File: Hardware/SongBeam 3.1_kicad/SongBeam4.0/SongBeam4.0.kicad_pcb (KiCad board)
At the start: 2 copper layers, 130 parts, among them J1 Conn_01x02, J10 732511150, J11 USB_B_Micro, J12 Conn_01x02, J13 Conn_01x02, J2 RJ45, J3 RJ45, J4 Conn_01x07, J5 Conn_01x04, J6 Conn_01x07, J7 Conn_01x09, J8 Conn_01x04, J9 Conn_01x08, SW2 PTS815 SJM 250 SMTR LFS, SW3 PTS815 SJM 250 SMTR LFS, U1 IM66D132H, U10 Teensy4.1, U11 BQ25185, U12 AO6604, U13 TPS62842DGRR, U14 TPL5111DDCR, U15 AO6604, U16 TXS0108EPW, U17 LP5907MFX-1.8/NOPB, U18 AO3407A, U19 MAX-M10M-00B, U2 IM66D132H, U3 IM66D132H, U4 IM66D132H, U5 IM66D132H, U6 IM66D132H, U7 IM66D132H, U8 IM66D132H, U9 PCMD3180IRTWR

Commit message: pcb savepoint
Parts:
- removed J13: Conn_01x02, Connector_PinHeader_1.00mm:PinHeader_1x02_P1.00mm_Horizontal
- added REF3: MountingHole_3.2mm_M3, MountingHole:MountingHole_3.2mm_M3, F.Cu at (193.5, 31.0)
- added REF3: MountingHole_3.2mm_M3, MountingHole:MountingHole_3.2mm_M3, F.Cu at (26.6, 30.9)
- added REF3: MountingHole_3.2mm_M3, MountingHole:MountingHole_3.2mm_M3, F.Cu at (26.7, 127.0)
- added REF3: MountingHole_3.2mm_M3, MountingHole:MountingHole_3.2mm_M3, F.Cu at (193.6, 127.0)
- CHG1: value ORANGE -> SFH2701; footprint LED_SMD:LED_0201_0603Metric -> LED_SMD:LED-APA102-2020
- D4, D5, D6: value MBRX120 -> MBRX120LF-TP
- Fault1: renamed from FAULT1; value RED -> SFH2701; footprint LED_SMD:LED_0201_0603Metric -> LED_SMD:LED-APA102-2020
- J10: footprint DFE201612E:1286ASH1R0MP2 -> 73251:CONN_73251-1150_MOL
- J11: value USB_B_Micro -> Conn_01x02; footprint 10118192:101181920002LF -> Connector_PinHeader_1.00mm:PinHeader_1x02_P1.00mm_Horizontal
- J7: value Conn_01x09 -> Conn_01x04; footprint Connector_PinHeader_1.00mm:PinHeader_1x09_P1.00mm_Horizontal -> Connector_PinHeader_1.00mm:PinHeader_1x04_P1.00mm_Horizontal
- J8: value Conn_01x04 -> Conn_01x08; footprint Connector_PinHeader_1.00mm:PinHeader_1x04_P1.00mm_Horizontal -> Connector_PinHeader_1.00mm:PinHeader_1x08_P1.00mm_Horizontal
- J9: value Conn_01x08 -> USB_B_Micro; footprint Connector_PinHeader_1.00mm:PinHeader_1x08_P1.00mm_Horizontal -> 10118192:101181920002LF
- U14: footprint TPL5111DDCR:TPL5111DDCR -> TPL5111DDCR:DDC0006A_L
- moved BAT1 218.0 mm to (58.7, 119.1), turned to 180 degrees
- moved J9 194.6 mm to (38.6, 92.7), turned to -90 degrees
- moved D2 185.1 mm to (66.2, 105.3), turned to 180 degrees
- moved SW3 177.1 mm to (111.4, 105.4), turned to 180 degrees
- moved U18 161.5 mm to (76.5, 105.4), turned to -90 degrees
- moved R39 146.6 mm to (73.0, 105.6), turned to 90 degrees
- moved U19 136.5 mm to (90.1, 115.6), turned to -90 degrees
- moved L2 132.2 mm to (88.0, 125.5), turned to 180 degrees
- moved C39 129.1 mm to (86.2, 122.1), turned to 180 degrees
- moved R18 124.1 mm to (130.4, 109.2), turned to -90 degrees
- moved U10 121.8 mm to (134.9, 122.2)
- moved R19 120.8 mm to (133.5, 109.2), turned to -90 degrees
- moved R20 117.5 mm to (136.7, 109.3), turned to -90 degrees
- moved C13 115.0 mm to (129.9, 64.6)
- moved C14 115.0 mm to (134.6, 69.9)
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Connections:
- CHG1 pad 1: (no net) -> Net-(CHG1-K)
- CHG1 pad 2: (no net) -> +5V
- D4 pad 1: (no net) -> Net-(D4-K)
- D4 pad 2: (no net) -> Net-(D4-A)
- D5 pad 1: (no net) -> Net-(D4-K)
- D5 pad 2: (no net) -> SLEEP_LATCH
- D6 pad 1: (no net) -> VBUS
- D6 pad 2: (no net) -> Net-(D6-A)
- Fault1 pad 1: (no net) -> Net-(Fault1-K)
- Fault1 pad 2: (no net) -> +5V
- J11 pad 1: Net-(J11-VBUS) -> VBUS
- J11 pad 2: unconnected-(J11-D--Pad2) -> GND
- J12 pad 1: VBUS -> VBAT
- J7 pad 1: GND -> SENSORSDA
- J7 pad 2: Done -> sensorSCL
- J7 pad 3: SHDNZ_3.3V -> GND
- J7 pad 4: SCL_MOSI_3.3V -> +3.3V
- J8 pad 1: SENSORSDA -> GPS_PWR
- J8 pad 2: sensorSCL -> GPS_ON
- J8 pad 3: GND -> TMPPS
- J8 pad 4: +3.3V -> TXGPS
- J9 pad 1: GPS_PWR -> Net-(D6-A)
- J9 pad 2: GPS_ON -> unconnected-(J9-D--Pad2)
- J9 pad 3: TMPPS -> unconnected-(J9-D+-Pad3)
- J9 pad 4: TXGPS -> unconnected-(J9-ID-Pad4)
- J9 pad 5: RXGPS -> GND
- R21 pad 2: Net-(CHG1-PadC) -> Net-(CHG1-K)
- R23 pad 2: Net-(FAULT1-PadC) -> Net-(Fault1-K)
- R34 pad 1: Net-(D4-PadC) -> Net-(D4-K)
- R36 pad 1: Net-(D4-PadA) -> Net-(D4-A)
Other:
- board outline added: 175.8 x 104.9 mm
- board text added: "1 xxx 1 xx xx 1 x x xxxxx 1 x x xxx xxx 1 x x xx xx 1 x x x x 1---x------------x--------x----------x------ 1 x x x x 1 x x x x 1 x x x x 1 x xx xx x 1x xxx 7777777777777777777777777777777777777777777777777777"
- board text added: "DAUGHTER BOARD A 1.0 \||||/ |||| /||||\ SONGBEAM 4.0"
- board text added: "SENSOR PORT"
- board text added: "TEENSY 4.1"

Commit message: prerouting
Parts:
- removed REF3 (x4): MountingHole_3.2mm_M3, MountingHole:MountingHole_3.2mm_M3
- CHG1: value SFH2701 -> SFH_2716_A01; footprint LED_SMD:LED-APA102-2020 -> LEDSB:LEDC2012X100N
- FAULT1: renamed from Fault1; value SFH2701 -> SFH_2716_A01; footprint LED_SMD:LED-APA102-2020 -> LEDSB:LEDC2012X100N
- J1, J11, J12: footprint Connector_PinHeader_1.00mm:PinHeader_1x02_P1.00mm_Horizontal -> Connector_PinHeader_1.00mm:PinHeader_1x02_P1.00mm_Vertical
- J4, J6: footprint Connector_PinHeader_1.00mm:PinHeader_1x07_P1.00mm_Horizontal -> Connector_PinHeader_1.00mm:PinHeader_1x07_P1.00mm_Vertical
- J5, J7: footprint Connector_PinHeader_1.00mm:PinHeader_1x04_P1.00mm_Horizontal -> Connector_PinHeader_1.00mm:PinHeader_1x04_P1.00mm_Vertical
- J8: footprint Connector_PinHeader_1.00mm:PinHeader_1x08_P1.00mm_Horizontal -> Connector_PinHeader_1.00mm:PinHeader_1x08_P1.00mm_Vertical
- moved J5 4.59 mm to (110.3, 43.4)
- moved CHG1 3.07 mm to (47.0, 96.8), turned to 90 degrees
- moved R27 2.00 mm to (55.6, 91.1)
- moved D7 2.00 mm to (59.3, 89.0)
- moved R24 2.00 mm to (52.6, 88.1)
- moved R25 2.00 mm to (54.8, 88.2)
- moved R26 2.00 mm to (57.0, 88.2)
- moved R28 2.00 mm to (64.6, 90.7)
- moved R29 2.00 mm to (61.7, 89.9)
- moved TP1 2.00 mm to (64.7, 87.2)
- moved U11 1.47 mm to (47.4, 92.7)
- moved FAULT1 1.41 mm to (47.9, 89.5)
- moved SW3 0.30 mm to (111.5, 105.1)
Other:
- board text added: "(+)"
- board text added: "(-)"
- board text added: "Battery type"
- board text added: "Data 1.8v debug"
- board text added: "Data 3.3v debug"
- board text added: "Daughter port 1"
- board text added: "Daughter port 2"
- board text added: "GNSS antena port"
- board text added: "GNSS debug"
- board text added: "Li Fe PO4"
- board text added: "MIC 1-2"
- board text added: "MIC 3-4"
- board text added: "MIC 5-6"
- board text added: "MIC 7-8"
- board text added: "MIC debug"
- board text added: "Na Ion"
- board text added: "Power debug"
- board text added: "SongBeam 4.0"
- board text removed: "1 xxx 1 xx xx 1 x x xxxxx 1 x x xxx xxx 1 x x xx xx 1 x x x x 1---x------------x--------x----------x------ 1 x x x x 1 x x x x 1 x x x x 1 x xx xx x 1x xxx 7777777777777777777777777777777777777777777777777777"
- board text removed: "DAUGHTER BOARD A 1.0 \||||/ |||| /||||\ SONGBEAM 4.0"

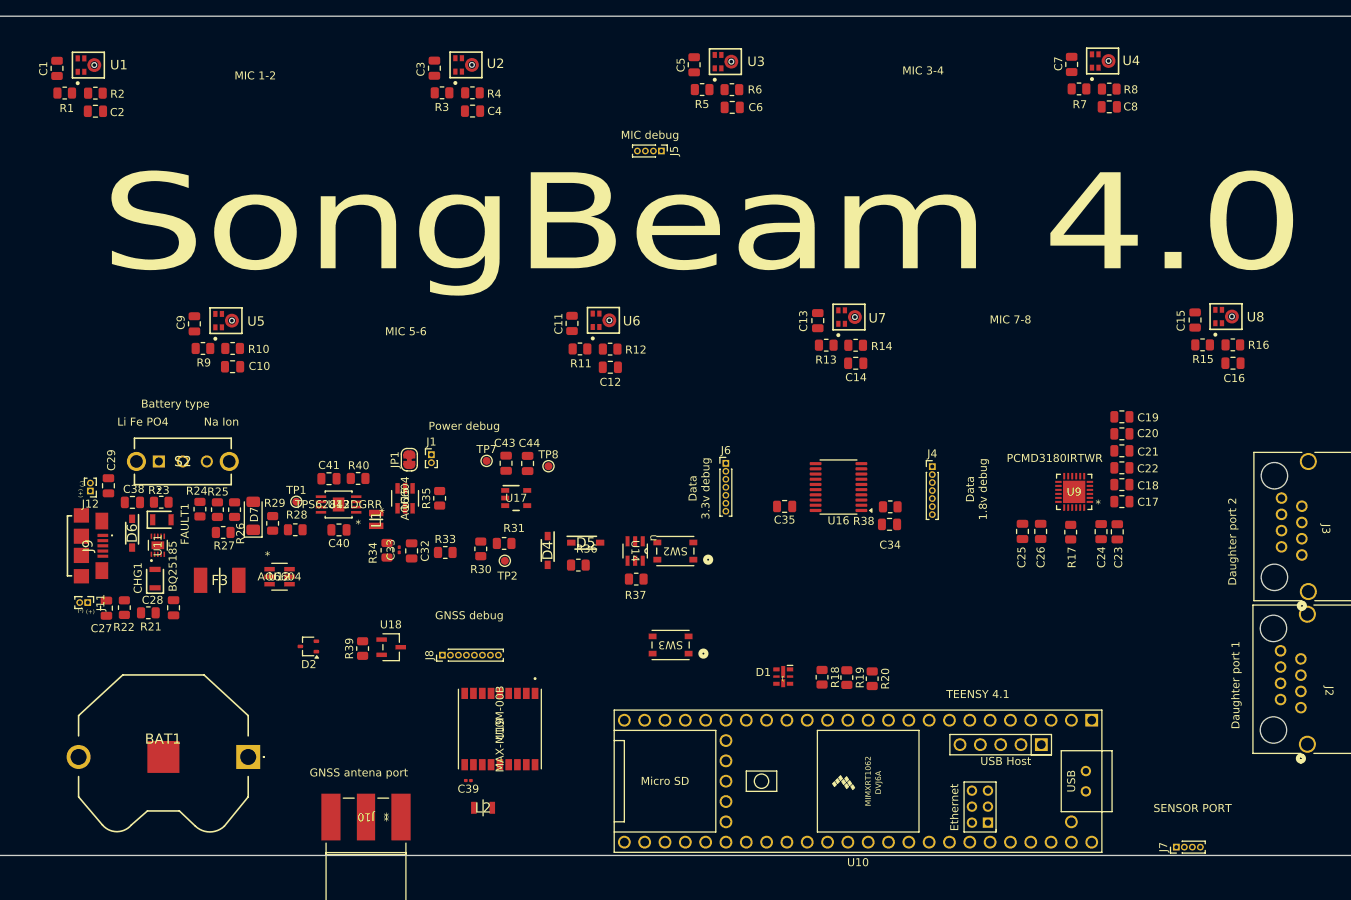
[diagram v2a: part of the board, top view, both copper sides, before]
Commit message: Tracing V1 SB4.0
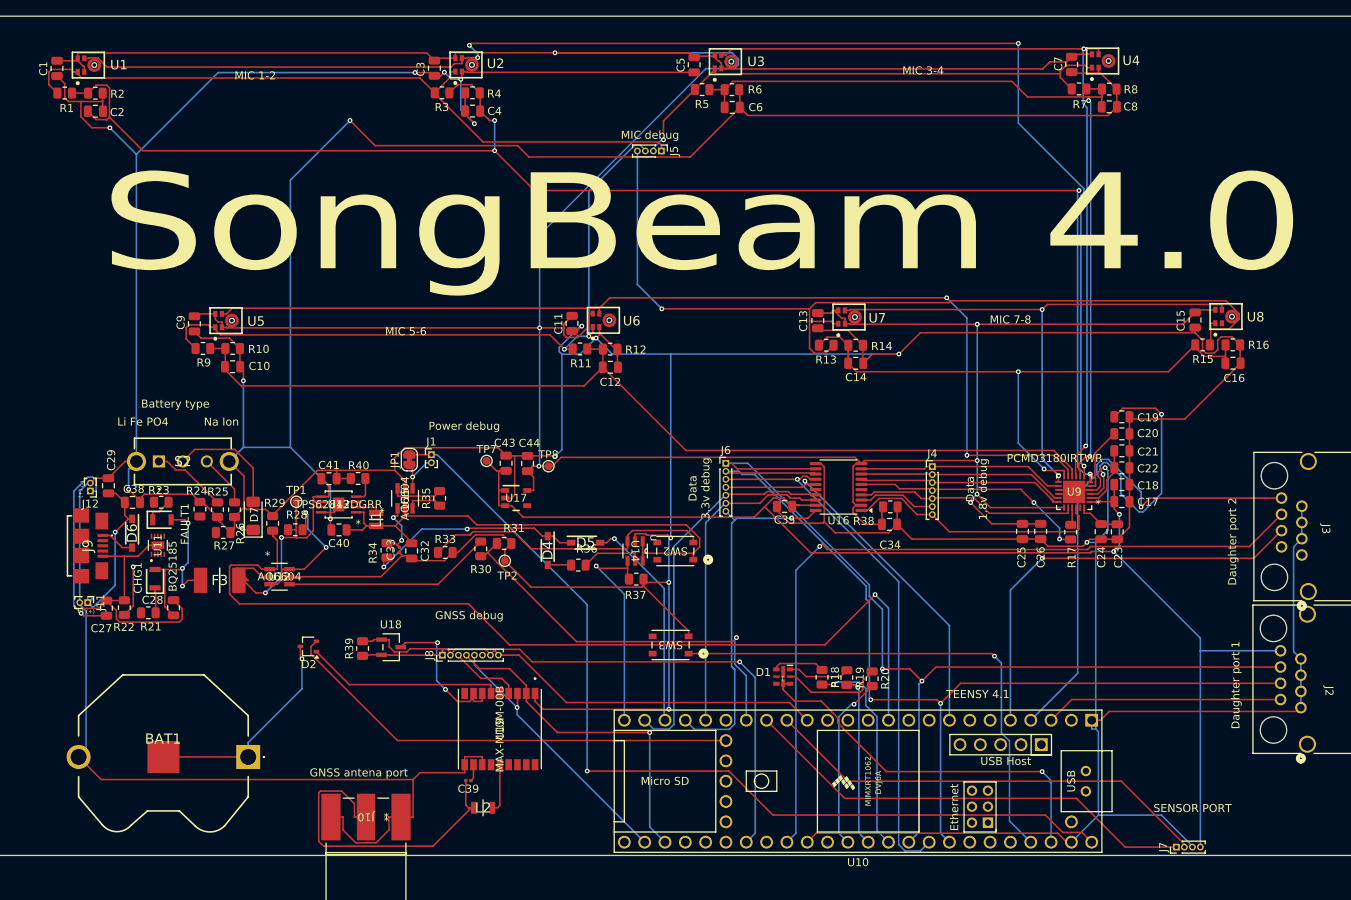
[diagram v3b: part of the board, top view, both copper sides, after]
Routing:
- net GND: track 0.00 -> 1106.5 mm, vias 0 -> 18
- net +1V8: track 0.00 -> 450.8 mm, vias 0 -> 7
- net micGRP_1out_1.8V: track 0.00 -> 187.7 mm, vias 0 -> 4
- net micgrp_1IN_1.8V: track 0.00 -> 179.1 mm, vias 0 -> 4
- net +3.3V: track 0.00 -> 160.3 mm, vias 0 -> 2
- net micGRP_3IN_1.8V: track 0.00 -> 127.0 mm, vias 0 -> 2
- net micGRP_3out_1.8V: track 0.00 -> 122.7 mm
- net SCL_MOSI_3.3V: track 0.00 -> 119.8 mm, vias 0 -> 2
- net SHDNZ_3.3V: track 0.00 -> 118.9 mm, vias 0 -> 2
- net PWR: track 0.00 -> 117.6 mm, vias 0 -> 1
- net emrg_pwr_swch: track 0.00 -> 117.1 mm, vias 0 -> 1
- net testGRP4: track 0.00 -> 114.6 mm, vias 0 -> 1
- net micGRP_2out_1.8V: track 0.00 -> 105.1 mm, vias 0 -> 2
- net micGRP_2IN_1.8V: track 0.00 -> 102.4 mm, vias 0 -> 2
- net MCLK_TDM2_3.3V: track 0.00 -> 98.6 mm, vias 0 -> 1
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
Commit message: Pcb bugfixxing
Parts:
- R25: value 6.8K -> 6.8k
- R26: value 5.1K -> 5.1k
- R27: value 10K -> 10k
- U11: value BQ25185 -> BQ25185DLHR
- U13: value TPS62842DGRR -> TPS62842
- U14: footprint TPL5111DDCR:DDC0006A_L -> TPL5111DDCR:SOT95P280X110-6N
- U9: value PCMD3180IRTWR -> PCMD3180
- moved R33 23.6 mm to (106.2, 88.0)
- moved R30 20.2 mm to (69.5, 101.8), turned to 0 degrees
- moved R31 17.5 mm to (75.9, 101.9)
- moved R34 16.2 mm to (91.7, 89.1), turned to 180 degrees
- moved J12 14.5 mm to (25.1, 81.6)
- moved J11 13.1 mm to (26.3, 104.4), turned to 0 degrees
- moved TP2 13.1 mm to (79.9, 102.0)
- moved J9 12.5 mm to (26.1, 92.9)
- moved D6 12.1 mm to (33.2, 86.1)
- moved C29 12.1 mm to (29.7, 81.5)
- moved U11 11.8 mm to (35.6, 94.0)
- moved S2 9.71 mm to (38.8, 77.9)
- moved R39 8.65 mm to (72.9, 114.2)
- moved D2 8.65 mm to (66.1, 114.0)
- moved U18 8.65 mm to (76.5, 114.0)
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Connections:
- R22 pad 1: GND -> Net-(U11-/CE)
- R22 pad 2: Net-(U11-/CE) -> GND
- R23 pad 1: Net-(U11-STAT1) -> Net-(FAULT1-K)
- R23 pad 2: Net-(FAULT1-K) -> Net-(U11-STAT1)
- R25 pad 1: GND -> Net-(R25-Pad1)
- R25 pad 2: Net-(R25-Pad2) -> GND
- R26 pad 1: GND -> Net-(R26-Pad1)
- R26 pad 2: Net-(R26-Pad2) -> GND
- S2 pad 1: Net-(R25-Pad2) -> Net-(R25-Pad1)
- S2 pad 3: Net-(R26-Pad2) -> Net-(R26-Pad1)
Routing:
- net GND: track 1106.5 -> 995.0 mm, vias 18 -> 52
- net emrg_pwr_swch: track 117.1 -> 90.5 mm, vias 1 -> 2
- net Net-(D7-K): track 1.45 -> 23.4 mm, vias 1 -> 2
- net Net-(U9-VREF): track 34.2 -> 12.4 mm
- net Net-(U14-DELAY_M_DRV): track 37.0 -> 15.8 mm
- net Net-(D4-K): track 27.6 -> 7.18 mm, vias 2 -> 0
- net antenna: track 39.9 -> 19.7 mm
- net Net-(U12-D2): track 26.1 -> 6.83 mm
- net testGRP4: track 114.6 -> 96.5 mm
- net Net-(R25-Pad1): track 0.00 -> 18.0 mm, vias 0 -> 1
- net +1V8: track 450.8 -> 434.0 mm, vias 7 -> 18
- net Net-(R26-Pad1): track 0.00 -> 16.1 mm, vias 0 -> 1
- net Net-(U11-STAT1): track 0.00 -> 16.1 mm
- net Net-(U11-ISET): track 0.00 -> 15.0 mm
- net GPS_PWR: track 60.1 -> 75.1 mm, vias 0 -> 1
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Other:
- board text added: "BATTERY"
- board text added: "For soloar either usb or pins"
- board text added: "POWER (timer)"
- board text added: "SOLAR"
- board text added: "battery % & SD card %"

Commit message: debugging
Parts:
- moved J2 1.50 mm to (190.4, 114.5)
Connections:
- R1 pad 1: TestGRP1 -> testGRP1
- U1 pad 1: TestGRP1 -> testGRP1
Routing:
- net GND: track 995.0 -> 1007.3 mm, vias 52 -> 50
- net emrg_pwr_swch: track 90.5 -> 93.2 mm
- net FSYNC_TDM2_3.3V: track 29.8 -> 30.5 mm
- net +3.3V: track 163.5 -> 162.9 mm
- net +1V8: track 434.0 -> 434.5 mm, vias 18 -> 19

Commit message: debug
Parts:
- added REF**: MountingHole_3.2mm_M3, MountingHole:MountingHole_3.2mm_M3, F.Cu at (25.8, 30.0)
- added REF**: MountingHole_3.2mm_M3, MountingHole:MountingHole_3.2mm_M3, F.Cu at (194.6, 30.0)
- added REF**: MountingHole_3.2mm_M3, MountingHole:MountingHole_3.2mm_M3, F.Cu at (25.8, 127.9)
- added REF**: MountingHole_3.2mm_M3, MountingHole:MountingHole_3.2mm_M3, F.Cu at (194.6, 127.9)
- moved C10 1.57 mm to (55.2, 70.2)
- moved C9 1.57 mm to (50.4, 64.9)
- moved R10 1.57 mm to (55.2, 68.0)
- moved R9 1.57 mm to (51.5, 68.0)
- moved U5 1.57 mm to (54.0, 64.5)
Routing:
- added copper zone on B.Cu, net GND
- added copper zone on F.Cu, net GND
